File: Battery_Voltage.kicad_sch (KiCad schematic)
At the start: 15 parts, among them IC3 AMC1350DWVR

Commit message: mini review notes
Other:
- note added: "V+ and V- not descriptive bruh"
- note added: "V_IN_1 change to output check all pins for in or out"
- note added: "V_IN_1 to V_IN_BAT to be more descriptive"
- note added: "change HVGND and LVGND global labels into just a hierarchal pin"
- note added: "hierarchal pin works like label"
- note added: "line with line tool and "e""
- note removed: "--------"
- moved on the sheet: TP16
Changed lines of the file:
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@@
+		)
+	)
+	(text "line with line tool and \"e\""
+		(exclude_from_sim no)
+		(at 109.855 60.325 0)
+		(effects
+			(font
+				(size 1.27 1.27)
+			)
 		)
 	)
@@
 		)
 	)
-	(text "--------\n"
-		(exclude_from_sim no)
-		(at 102.87 38.608 90)
-		(effects
-			(font
-				(size 1.27 1.27)
-			)
-		)
-	)
 	(text "Vin = HV x Rbot / (Rtop + Rbot)\nRtop = 4 x 100k = 400k\nRbot = 10k\n\nVin = HV x 10k / (400k + 10k) = HV x 0.02439\n\nHV = 100V -> Vin = 2.44V\nHV = 120V -> Vin = 2.93V\nHV = 130V -> Vin = 3.17V\n\nAmp linear input range: +/-5V (AMC1350)\nDivider current at 130V: 130V / 410k = 0.32mA\nPer top resistor: ~32V, ~10mW\nAmp input (1.25M) loads Rbot ~0.8%: correct in firmware"
 		(exclude_from_sim no)
@@
 		)
 	)
+	(text "V+ and V- not descriptive bruh"
+		(exclude_from_sim no)
+		(at 123.825 28.575 0)
+		(effects
+			(font
+				(size 1.27 1.27)
+			)
+		)
+	)
+	(text "change HVGND and LVGND global labels into just a hierarchal pin"
+		(exclude_from_sim no)
+		(at 198.12 38.1 0)
+		(effects
+			(font
+				(size 1.27 1.27)
+			)
+		)
+	)
+	(text "V_IN_1 to V_IN_BAT to be more descriptive"
+		(exclude_from_sim no)
+		(at 33.655 90.805 0)
+		(effects
+			(font
+				(size 1.27 1.27)
+			)
+		)
+	)
+	(text "V_IN_1 change to output\ncheck all pins for in or out"
+		(exclude_from_sim no)
+		(at 35.56 58.42 0)
+		(effects
+			(font
+				(size 1.27 1.27)
+			)
+		)
+	)
+	(text "hierarchal pin works like label"
+		(exclude_from_sim no)
+		(at 81.28 29.21 0)
+		(effects
+			(font
+				(size 1.27 1.27)
+			)
+		)
+	)
+	(junction
+		(at 140.335 33.655)
+		(diameter 0)
+		(color 0 0 0 0)
+	)
+	(junction
+		(at 30.48 68.58)
+		(diameter 0)
+		(color 0 0 0 0)
+	)
+	(junction
+		(at 21.59 68.58)
+		(diameter 0)
+		(color 0 0 0 0)
+	)
+	(junction
+		(at 140.335 25.4)
+		(diameter 0)
+		(color 0 0 0 0)
+	)
+	(junction
+		(at 65.405 33.655)
+		(diameter 0)
+		(color 0 0 0 0)
+	)
+	(junction
+		(at 21.59 80.01)
+		(diameter 0)
+		(color 0 0 0 0)
+	)
+	(junction
+		(at 65.405 42.545)
+		(diameter 0)
+		(color 0 0 0 0)
+	)
 	(junction
 		(at 65.405 30.48)
@@
 	)
 	(junction
-		(at 140.335 33.655)
+		(at 140.335 42.545)
 		(diameter 0)
 		(color 0 0 0 0)
 	)
 	(junction
-		(at 30.48 68.58)
-		(diameter 0)
-		(color 0 0 0 0)
-	)
-	(junction
-		(at 21.59 68.58)
-		(diameter 0)
-		(color 0 0 0 0)
-	)
-	(junction
-		(at 140.335 30.48)
-		(diameter 0)
-		(color 0 0 0 0)
-	)
-	(junction
-		(at 65.405 33.655)
-		(diameter 0)
-		(color 0 0 0 0)
-	)
-	(junction
-		(at 21.59 80.01)
-		(diameter 0)
-		(color 0 0 0 0)
-	)
-	(junction
-		(at 65.405 42.545)
-		(diameter 0)
-		(color 0 0 0 0)
-	)
-	(junction
-		(at 140.335 42.545)
+		(at 120.65 36.83)
 		(diameter 0)
 		(color 0 0 0 0)
@@
 	(wire
 		(pts
+			(xy 65.405 30.48) (xy 88.9 30.48)
+		)
+		(stroke
+			(width 0)
+			(type default)
+		)
+	)
+	(wire
+		(pts
 			(xy 88.9 50.165) (xy 88.9 41.91)
 		)
@@
 		)
 	)
-	(wire
-		(pts
-			(xy 140.335 30.48) (xy 140.335 33.655)
-		)
-		(stroke
-			(width 0)
-			(type default)
+	(polyline
+		(pts
+			(xy 102.87 20.32) (xy 102.87 56.515)
+		)
+		(stroke
+			(width 0)
+			(type dash)
 		)
 	)
@@
 	(wire
 		(pts
-			(xy 116.84 30.48) (xy 116.84 34.29)
+			(xy 116.84 25.4) (xy 116.84 34.29)
 		)
 		(stroke
@@
 	(wire
 		(pts
-			(xy 120.015 36.83) (xy 116.84 36.83)
+			(xy 116.84 36.83) (xy 120.65 36.83)
 		)
 		(stroke
@@
 	(wire
 		(pts
+			(xy 65.405 30.48) (xy 65.405 33.655)
+		)
+		(stroke
+			(width 0)
+			(type default)
+		)
+	)
+	(wire
+		(pts
 			(xy 21.59 66.04) (xy 21.59 68.58)
 		)
@@
 	(wire
 		(pts
-			(xy 140.335 25.4) (xy 140.335 30.48)
+			(xy 140.335 25.4) (xy 140.335 33.655)
 		)
 		(stroke
@@
 	(wire
 		(pts
-			(xy 125.73 38.735) (xy 120.015 38.735)
-		)
-		(stroke
-			(width 0)
-			(type default)
-		)
-	)
-	(wire
-		(pts
-			(xy 65.405 30.48) (xy 88.9 30.48)
-		)
-		(stroke
-			(width 0)
-			(type default)
-		)
-	)
-	(wire
-		(pts
-			(xy 125.73 36.83) (xy 125.73 38.735)
+			(xy 120.65 36.83) (xy 120.65 35.56)
 		)
 		(stroke
@@
 	(wire
 		(pts
+			(xy 120.65 36.83) (xy 127 36.83)
+		)
+		(stroke
+			(width 0)
+			(type default)
+		)
+	)
+	(wire
+		(pts
 			(xy 68.58 45.72) (xy 68.58 50.165)
 		)
@@
 	(wire
 		(pts
-			(xy 65.405 25.4) (xy 65.405 33.655)
+			(xy 65.405 25.4) (xy 65.405 30.48)
 		)
 		(stroke
@@
 	(wire
 		(pts
-			(xy 71.755 33.655) (xy 85.725 33.655)
+			(xy 76.835 33.655) (xy 85.725 33.655)
 		)
 		(stroke
@@
 	(wire
 		(pts
-			(xy 120.015 36.83) (xy 120.015 38.735)
-		)
-		(stroke
-			(width 0)
-			(type default)
-		)
-	)
-	(wire
-		(pts
-			(xy 116.84 30.48) (xy 140.335 30.48)
+			(xy 116.84 25.4) (xy 140.335 25.4)
 		)
 		(stroke
@@
 			(width 0)
 			(type default)
-		)
-	)
-	(label "V_IN_1"
-		(at 38.1 68.58 180)
-		(effects
-			(font
-				(size 1.27 1.27)
-			)
-			(justify right bottom)
-		)
-	)
-	(label "V_IN_1"
-		(at 71.755 33.655 0)
-		(effects
-			(font
-				(size 1.27 1.27)
-			)
-			(justify left bottom)
 		)
 	)
@@
 	(hierarchical_label "V1+"
 		(shape input)
-		(at 125.73 38.1 0)
+		(at 127 36.83 0)
 		(effects
 			(font
@@
 	)
 	(hierarchical_label "V_IN_1"
-		(shape input)
+		(shape output)
 		(at 38.1 68.58 0)
 		(effects
@@
 		)
 	)
+	(hierarchical_label "V_IN_1"
+		(shape output)
+		(at 76.835 33.655 180)
+		(effects
+			(font
+				(size 1.27 1.27)
+			)
+			(justify right)
+		)
+	)
 	(symbol
 		(lib_id "Device:C")
@@
 		(in_pos_files yes)
 		(dnp no)
-		(property "Reference" "#PWR042"
+		(property "Reference" "#PWR043"
 			(at 140.335 29.21 0)
 			(hide yes)
@@
 			(project "PS-PrechargeBoard"
 				(path "/74d17fe6-68d4-4bd7-954a-e2bbb58b1f1e/ad0f3840-ec25-4ea7-b025-1d3129a06533/c44cc650-ec3c-42a9-ae3c-bb53bdf38e25"
-					(reference "#PWR042")
+					(reference "#PWR043")
 					(unit 1)
 				)
@@
 		(in_pos_files yes)
 		(dnp no)
-		(property "Reference" "#PWR043"
+		(property "Reference" "#PWR044"
 			(at 140.335 57.15 0)
 			(hide yes)
@@
 			(project "PS-PrechargeBoard"
 				(path "/74d17fe6-68d4-4bd7-954a-e2bbb58b1f1e/ad0f3840-ec25-4ea7-b025-1d3129a06533/c44cc650-ec3c-42a9-ae3c-bb53bdf38e25"
-					(reference "#PWR043")
+					(reference "#PWR044")
 					(unit 1)
 				)
@@
 		(in_pos_files yes)
 		(dnp no)
-		(property "Reference" "#PWR041"
+		(property "Reference" "#PWR042"
 			(at 73.025 50.8 0)
 			(hide yes)
@@
 			(project "PS-PrechargeBoard"
 				(path "/74d17fe6-68d4-4bd7-954a-e2bbb58b1f1e/ad0f3840-ec25-4ea7-b025-1d3129a06533/c44cc650-ec3c-42a9-ae3c-bb53bdf38e25"
-					(reference "#PWR041")
+					(reference "#PWR042")
 					(unit 1)
 				)
@@
 		(in_pos_files yes)
 		(dnp no)
-		(property "Reference" "#PWR038"
+		(property "Reference" "#PWR039"
 			(at 21.59 87.63 0)
 			(hide yes)
@@
 			(project "PS-PrechargeBoard"
 				(path "/74d17fe6-68d4-4bd7-954a-e2bbb58b1f1e/ad0f3840-ec25-4ea7-b025-1d3129a06533/c44cc650-ec3c-42a9-ae3c-bb53bdf38e25"
-					(reference "#PWR038")
+					(reference "#PWR039")
 					(unit 1)
 				)
@@
 		(in_pos_files yes)
 		(dnp no)
-		(property "Reference" "#PWR039"
+		(property "Reference" "#PWR040"
 			(at 65.405 29.21 0)
 			(hide yes)
@@
 			(project "PS-PrechargeBoard"
 				(path "/74d17fe6-68d4-4bd7-954a-e2bbb58b1f1e/ad0f3840-ec25-4ea7-b025-1d3129a06533/c44cc650-ec3c-42a9-ae3c-bb53bdf38e25"
-					(reference "#PWR039")
+					(reference "#PWR040")
 					(unit 1)
 				)
@@
 		(in_pos_files yes)
 		(dnp no)
-		(property "Reference" "#PWR040"
+		(property "Reference" "#PWR041"
 			(at 65.405 57.15 0)
 			(hide yes)
@@
 			(project "PS-PrechargeBoard"
 				(path "/74d17fe6-68d4-4bd7-954a-e2bbb58b1f1e/ad0f3840-ec25-4ea7-b025-1d3129a06533/c44cc650-ec3c-42a9-ae3c-bb53bdf38e25"
-					(reference "#PWR040")
+					(reference "#PWR041")
 					(unit 1)
 				)
@@
 	(symbol
 		(lib_id "Connector:TestPoint")
-		(at 125.73 36.83 0)
+		(at 120.65 35.56 0)
 		(unit 1)
 		(body_style 1)
@@
 		(dnp no)
 		(property "Reference" "TP16"
-			(at 127 33.655 0)
+			(at 121.92 32.385 0)
 			(show_name no)
 			(do_not_autoplace no)
@@
 		)
 		(property "Value" "V+"
-			(at 127 36.195 0)
+			(at 121.92 34.925 0)
 			(show_name no)
 			(do_not_autoplace no)
@@
 		)
 		(property "Footprint" ""
-			(at 130.81 36.83 0)
+			(at 125.73 35.56 0)
 			(hide yes)
 			(show_name no)
@@
 		)
 		(property "Datasheet" ""
-			(at 130.81 36.83 0)
+			(at 125.73 35.56 0)
 			(hide yes)
 			(show_name no)
@@
 		)
 		(property "Description" "test point"
-			(at 125.73 36.83 0)
-			(hide yes)
-			(show_name no)
+			(at 120.65 35.56 0)
+			(hide yes)
+			(show_name no)

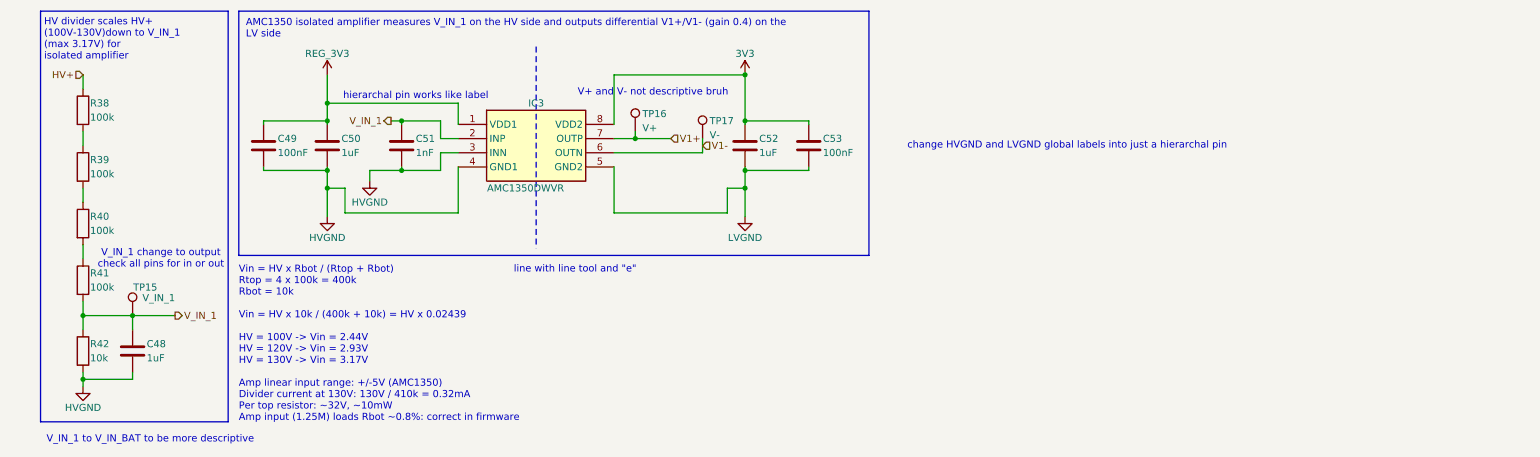
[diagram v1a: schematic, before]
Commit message: fixed battery voltage & motor voltage
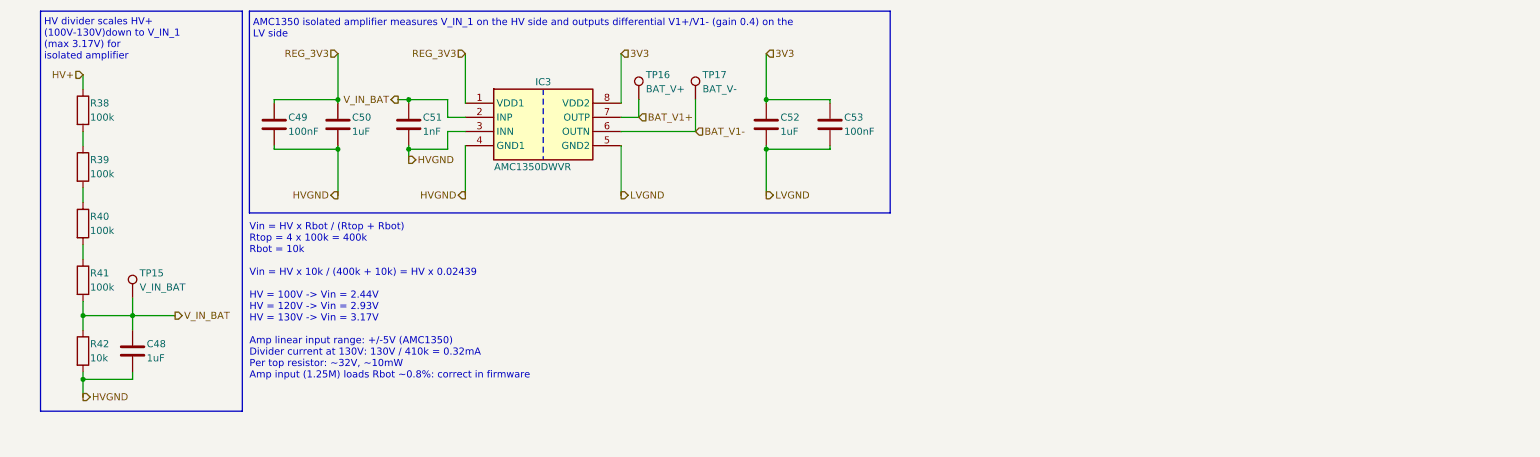
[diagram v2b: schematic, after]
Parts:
- removed TP15: V_IN_1, symbol Connector:TestPoint
- removed TP16: V+, symbol Connector:TestPoint
- removed TP17: V-, symbol Connector:TestPoint
- added TP15: V_IN_BAT, TestPoint:TestPoint_Loop_D1.80mm_Drill1.0mm_Beaded, symbol lhrs_misc:Multimeter_TP
- added TP16: BAT_V+, TestPoint:TestPoint_Loop_D1.80mm_Drill1.0mm_Beaded, symbol lhrs_misc:Multimeter_TP
- added TP17: BAT_V-, TestPoint:TestPoint_Loop_D1.80mm_Drill1.0mm_Beaded, symbol lhrs_misc:Multimeter_TP
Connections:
- net V1+ renamed BAT_V1+
- net BAT_V1+: now also TP16.1
- net V1- renamed BAT_V1-
- net BAT_V1-: now also TP17.1
- net V_IN_1 renamed V_IN_BAT
- net V_IN_BAT: now also TP15.1
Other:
- note removed: "V+ and V- not descriptive bruh"
- note removed: "V_IN_1 change to output check all pins for in or out"
- note removed: "V_IN_1 to V_IN_BAT to be more descriptive"
- note removed: "change HVGND and LVGND global labels into just a hierarchal pin"
- note removed: "hierarchal pin works like label"
- note removed: "line with line tool and "e""
- moved on the sheet: C49, C50, C51, C52, C53, IC3

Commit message: fixed lv
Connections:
- net BAT_V1+ renamed BAT_V+
- net BAT_V1- renamed BAT_V-
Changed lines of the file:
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@@
 		)
 	)
-	(hierarchical_label "BAT_V1+"
+	(hierarchical_label "BAT_V+"
 		(shape input)
 		(at 121.285 33.02 0)
@@
 		)
 	)
-	(hierarchical_label "BAT_V1-"
+	(hierarchical_label "BAT_V-"
 		(shape input)
 		(at 131.445 35.56 0)

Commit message: shifted hierarchical sheets
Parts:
- renumbered C52 to C?, C49 to C?, C48 to C?, C53 to C?, C51 to C?, C50 to C?, IC3 to IC?, R41 to R?, R40 to R?, R38 to R?, R39 to R?, R42 to R?, TP16 to TP?, TP15 to TP?, TP17 to TP?
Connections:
- net 3V3: no longer IC?.8 (VDD2)
- net LVGND: no longer IC?.5 (GND2)
- new net 3V3A: IC?.8 (VDD2)
- new net GNDA: IC?.5 (GND2)
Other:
- moved on the sheet: C?, IC?, TP?

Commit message: unboxed items to be fixed later
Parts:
- added C?: 10nF, symbol Device:C
- added C?: 1uF, Capacitor_SMD:C_0603_1608Metric_Pad1.08x0.95mm_HandSolder, symbol Device:C
- added R? (x2): 10k, symbol Device:R
- added R? (x2): 10k, Package_DIP:DIP-8_W7.62mm, symbol Device:R
- added R?: 10, symbol Device:R
- added TP?: V_OUT_BAT, TestPoint:TestPoint_Loop_D1.80mm_Drill1.0mm_Beaded, symbol lhrs_misc:Multimeter_TP
- added U? (x2): TLV9002QDRQ1, Package_SO:SOIC-8_3.9x4.9mm_P1.27mm, symbol UTSVT-Misc:TLV9002QDRQ1
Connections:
- net 3V3: now also C?.1, U?.8 (V+)
- net BAT_V+: now also R?.1
- net BAT_V-: now also R?.1
- net LVGND: now also C?.2, C?.2, R?.2, U?.4 (V-)
- new net: R?.1, R?.2, U?.1
- new net: R?.1, R?.2, U?.2 (-)
- new net: R?.1, R?.2, U?.3 (+)
- new net V_OUT_BAT: C?.1, R?.2, TP?.1
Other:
- note added: "Op-amps acting as a unity gain amplifier"
- note added: "make universal in hieracvrchal pin"

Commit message: added DE1a-12V precharge relay
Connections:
- net LVGND: no longer C?.2, C?.2, C?.2, C?.2, U?.4 (V-)
- net GNDA renamed GND
- net GND: now also C?.2, C?.2, C?.2, C?.2, U?.4 (V-)
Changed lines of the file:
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@@
 		)
 	)
-	(hierarchical_label "LVGND"
+	(hierarchical_label "GND"
 		(shape bidirectional)
 		(at 138.43 46.99 0)
@@
 		)
 	)
-	(hierarchical_label "GNDA"
+	(hierarchical_label "GND"
 		(shape bidirectional)
 		(at 112.395 46.99 0)
@@
 			)
 		)
-		(property "Value" "LVGND"
+		(property "Value" "GND"
 			(at 235.585 79.375 0)
 			(show_name no)
@@
 			)
 		)
-		(property "Value" "LVGND"
+		(property "Value" "GND"
 			(at 260.985 74.93 0)
 			(show_name no)

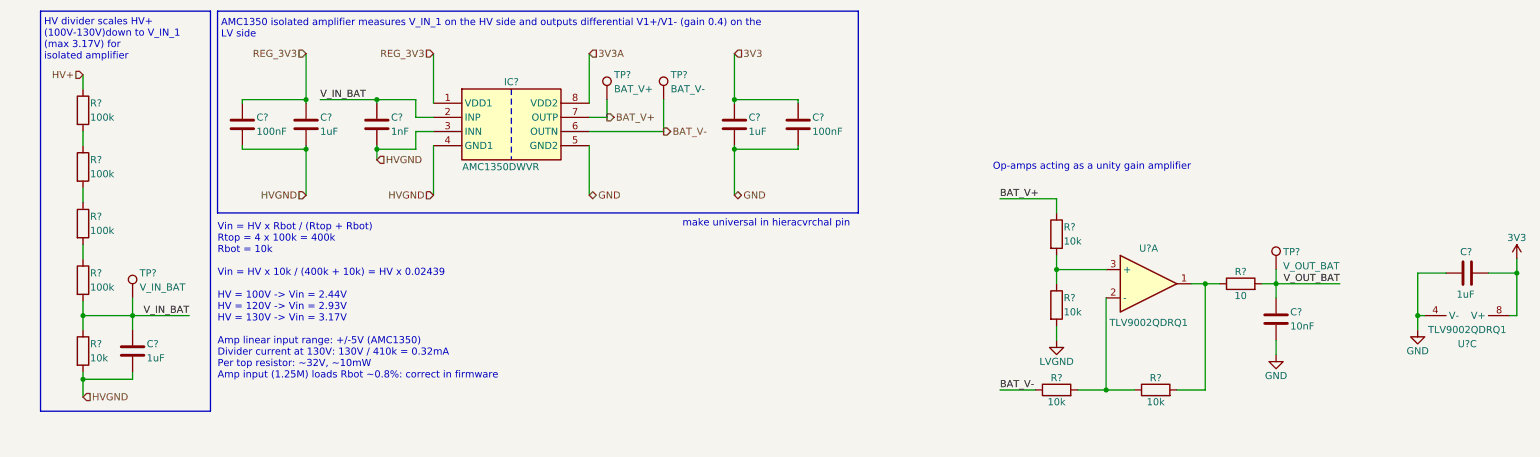
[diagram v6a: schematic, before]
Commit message: V_OUT_BAT & V_OUT_MOT & PRECHARGE_CTRL to MCU
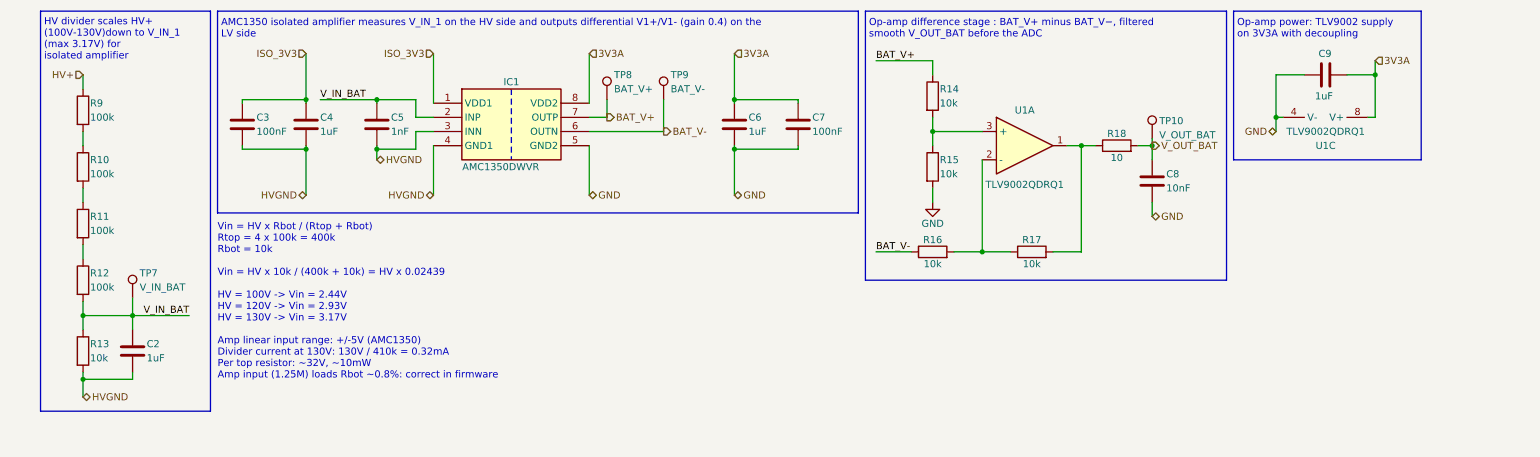
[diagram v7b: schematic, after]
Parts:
- gave numbers to parts that had none: 24
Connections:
- net 3V3 is gone; now on net 3V3A: C6.1, C7.1, C9.1, U1.8 (V+)
- net LVGND is gone; now on net GND: R15.2
- net REG_3V3 renamed ISO_3V3
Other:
- note added: "Op-amp difference stage : BAT_V+ minus BAT_V−, filtered smooth V_OUT_BAT before the ADC"
- note added: "Op-amp power: TLV9002 supply on 3V3A with decoupling"
- note removed: "Op-amps acting as a unity gain amplifier"
- note removed: "make universal in hieracvrchal pin"
- moved on the sheet: C8, C9, R14, R15, R16, R17, R18, TP10, U1A, U1C
